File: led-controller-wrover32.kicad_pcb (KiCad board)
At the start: 4 copper layers, 36 x 40 mm, 123 parts, among them J101 Micro USB, J102 UART, J103 STATUS OUT, J104 USB_B_Micro, J105 POWER IN, J107 I2C, J108 5V_LOGIC, J303 Micro_SD_Card, J304 Speaker, J401 Fan PWM, J402 GPIO_CONN, J409 12V_OUT, Q101 UMH3N, Q102 BSS138, Q103 EM6K7T2R, Q303 BSS138, Q401 SIL2301-TP, Q402 EM6K7T2R, SW301 KMR2, SW302 KMR2, U102 USBUF02W6, U103 ESP32-S3-WROOM-2-N32R8V, U104 MAX3379EETD, U105 AP22815AWT-7, U201 XCL220, U301 SSM2518CPZ, U401 BNO085, U402 PCA9575HF, U405 TPS55340-Q1, Y401 OM-7604-C7

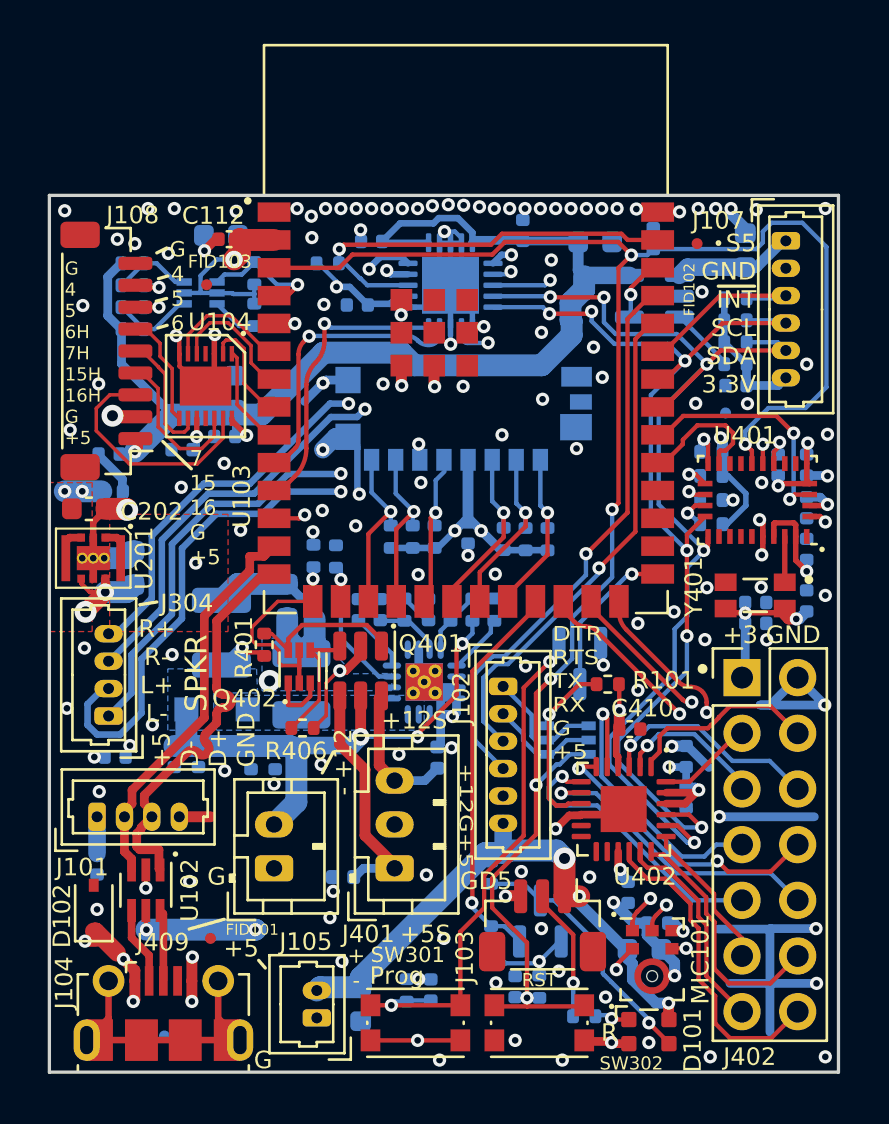
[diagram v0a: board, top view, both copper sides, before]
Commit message: More updates
- Changed obsolete unidirectional level shifter to open-collector level shifter
- Replaced BSS138 level shifters with dedicated level shifter
- Changed all 5V I/O pins to have 33 ohm resistor in series
- Changed a few capacitors
- Cleanup tracks, vias, silkscreen, etc.

Signed-off-by: Aaron Williams <aaron.w2@gmail.com>
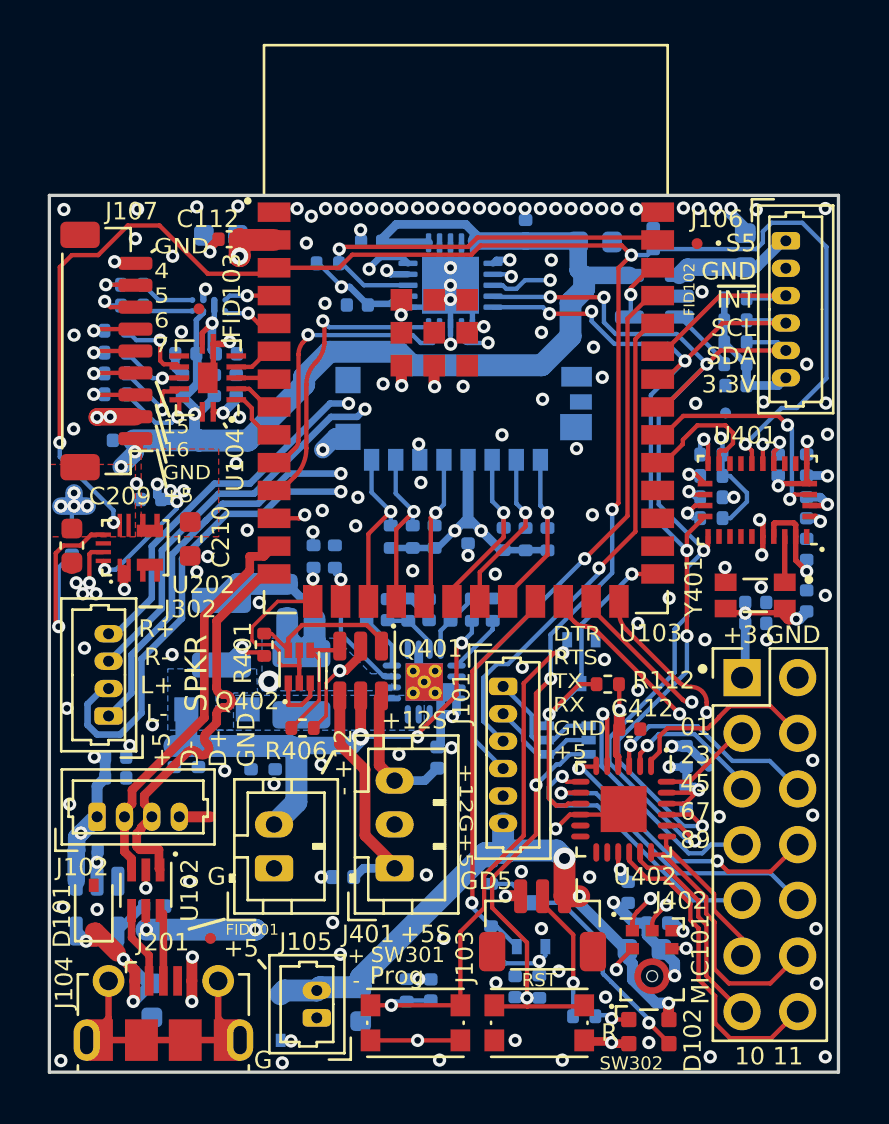
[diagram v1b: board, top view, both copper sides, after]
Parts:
- removed the C108 at (68.5, 39.0)
- removed the C201 at (63.9, 47.0)
- removed the C202 at (61.8, 44.3)
- removed Q103: EM6K7T2R, Package_TO_SOT_SMD:SOT-563
- removed the R109 at (69.3, 33.5)
- removed the R110 at (63.8, 33.1)
- removed the R112 at (69.3, 35.5)
- removed the R113 at (63.8, 36.1)
- removed the U201 at (62.0, 46.5)
- added C103: 0.1uF, Capacitor_SMD:C_0402_1005Metric, B.Cu at (61.7, 59.9)
- added C104: 10uF, Capacitor_SMD:C_0603_1608Metric, B.Cu at (64.7, 66.7)
- added C105: 0.1uF, Capacitor_SMD:C_0402_1005Metric, B.Cu at (64.8, 62.4)
- added C110: 1uF, Capacitor_SMD:C_0402_1005Metric, B.Cu at (66.1, 38.7)
- added C115: 1uF, Capacitor_SMD:C_0402_1005Metric, B.Cu at (68.1, 37.2)
- added C116: 1uF, Capacitor_SMD:C_0402_1005Metric, B.Cu at (66.2, 37.2)
- added C209: 22uF, Capacitor_SMD:C_0603_1608Metric, F.Cu at (61.0, 46.0)
- added C210: 22uF, Capacitor_SMD:C_0603_1608Metric, F.Cu at (66.4, 45.7)
- added D103: UDD32C12L01, Diode_SMD:D_SOD-323, B.Cu at (70.5, 67.5)
- added R104: 33, Resistor_SMD:R_0402_1005Metric, B.Cu at (63.0, 39.1)
- added R105: 33, Resistor_SMD:R_0402_1005Metric, B.Cu at (63.0, 38.1)
- added R106: 33, Resistor_SMD:R_0402_1005Metric, B.Cu at (63.0, 37.2)
- added R107: 33, Resistor_SMD:R_0402_1005Metric, B.Cu at (63.0, 36.2)
- added R206: 10K, Resistor_SMD:R_0402_1005Metric, B.Cu at (61.0, 45.9)
- added U101: AP2191WG-7, Package_TO_SOT_SMD:SOT-23-5, B.Cu at (62.2, 62.4)
- added U106: TCA9406ZYPR, Package_BGA:Texas_DSBGA-8_0.9x1.9mm_Layout2x4_P0.5mm, B.Cu at (67.3, 35.0)
- added U202: MPM3810GQB-33, Package_DFN_QFN:Monolithic_QFN-12-2.5x3.0mm_P0.4mm, F.Cu at (63.9, 46.1)
- J102: renamed from J101; value Micro USB -> USB
- Q102: footprint Package_TO_SOT_SMD:SOT-23 -> Package_TO_SOT_SMD:SOT-323_SC-70
- Q301: renamed from Q303; footprint Package_TO_SOT_SMD:SOT-23 -> Package_TO_SOT_SMD:SOT-323_SC-70
- R113: renamed from R111; value 22 -> 33
- R114: value 22 -> 33
- U104: value MAX3379EETD -> NTS0104BQ,115; footprint Aaron:TDFN-14_3x3mm_P0.4mm_EP1.78x2.35mm -> Package_TO_SOT_SMD:SOT-762-1
- U402: footprint Package_DFN_QFN:HVQFN-24-1EP_4x4mm_P0.5mm_EP2.1x2.1mm -> Aaron:HWQFN-24_EP_4x4_Pitch0.5mm
- moved C106 4.02 mm to (63.0, 56.6), turned to 0 degrees
- moved C108 3.83 mm to (68.5, 38.7), turned to 90 degrees
- moved C109 2.37 mm to (67.5, 38.7), turned to 90 degrees
- moved C211 1.79 mm to (64.6, 43.9), turned to 180 degrees
- moved FID103 1.15 mm to (66.8, 35.2)
- moved FID105 1.08 mm to (66.3, 68.3)
- moved R114 1.03 mm to (63.8, 34.1), turned to 0 degrees
- moved R113 0.93 mm to (63.8, 35.0), turned to 0 degrees
- moved C118 0.90 mm to (63.4, 41.2)
- moved Q102 0.46 mm to (82.0, 63.3)
- moved U104 0.39 mm to (67.2, 38.3), turned to 90 degrees
- moved C206 0.38 mm to (74.5, 48.9)
- moved C207 0.33 mm to (75.4, 48.9)
- moved R405 0.27 mm to (90.2, 44.7)
- moved R205 0.17 mm to (76.4, 48.9)
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- renumbered C116 to C101, C104 to C102, C105 to C106, C106 to C107, C110 to C108, C115 to C117, C117 to C118, C416 to C201, C417 to C202, C418 to C203, C419 to C204, C420 to C205, C421 to C206, C422 to C207, C423 to C208, C203 to C211, C314 to C301, C315 to C302, C316 to C303, C303 to C304, C318 to C305, C301 to C306, C302 to C307, C319 to C308, C412 to C410, C413 to C411, C410 to C412, C411 to C413, D102 to D101, D101 to D102, D402 to D201, D403 to D402, J102 to J101, J107 to J106, J108 to J107, J409 to J201, J303 to J301, J304 to J302, L401 to L201, R102 to R101, R103 to R102, R104 to R103, R105 to R109, R106 to R110, R107 to R111, R101 to R112, R416 to R201, R115 to R202, R417 to R203, R418 to R204, R419 to R205, R308 to R301, R309 to R305, R305 to R306, R306 to R307, R307 to R308, R301 to R309, U405 to U201
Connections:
- net /DO renamed /STS_DO
- net /IO2 renamed /SW_5V_EN
- net /IO46_5V renamed /STS_5V
- C101 pad 1: PVDD -> +5V
- C102 pad 1: PVDD -> +5V
- C106 pad 1: PVDD -> +5V
- C107 pad 1: PVDD -> +5V
- C109 pad 1: PVDD -> +5V
- C118 pad 1: PVDD -> +5V
- C204 pad 1: PVDD -> +5V
- C205 pad 1: PVDD -> +5V
- C305 pad 1: PVDD -> +5V
- C306 pad 1: PVDD -> +5V
- C307 pad 1: PVDD -> +5V
- D101 pad 1: PVDD -> VBUS
- D102 pad 4: PVDD -> +5V
- J101 pad 6: PVDD -> +5V
- J102 pad 1: PVDD -> +5V
- J103 pad 1: PVDD -> +5V
- J104 pad 1: PVDD -> VBUS
- J105 pad 2: PVDD -> +5V
- J107 pad 1: PVDD -> +5V
- L201 pad 1: PVDD -> +5V
- Q401 pad 2: PVDD -> +5V
- R102 pad 2: PVDD -> +5V
- R113 pad 1: /IO4_H -> /IO5_H
- R114 pad 1: /IO5_H -> /IO4_H
- R406 pad 1: PVDD -> +5V
- U104 pad 1: IO16 -> +3V3
- U104 pad 10: +3V3 -> Net-(R107-Pad2)
- U104 pad 11: unconnected-(U104-Pad11) -> Net-(R106-Pad2)
- U104 pad 12: /IO15_H -> Net-(R105-Pad2)
- U104 pad 13: /IO16_H -> Net-(R104-Pad2)
- U104 pad 14: PVDD -> +5V
- U104 pad 2: /IO15 -> IO16
- U104 pad 3: GND -> /IO15
- U104 pad 4: unconnected-(U104-Pad4) -> /IO7
- U104 pad 5: /IO7 -> /IO6
- U104 pad 6: /IO6 -> unconnected-(U104-Pad6)
- U104 pad 8: /IO6_H -> +3V3
- U104 pad 9: /IO7_H -> unconnected-(U104-Pad9)
- U105 pad 5: PVDD -> +5V
- U201 pad 2: PVDD -> +5V
- U301 pad 16: PVDD -> +5V
- U301 pad 20: PVDD -> +5V
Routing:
- net PVDD: track 99.4 -> 0.00 mm, vias 13 -> 0
- net +5V: track 0.00 -> 96.9 mm, vias 0 -> 14
- net GND: track 106.1 -> 70.1 mm, vias 143 -> 159
- net ~{RESET}: track 85.4 -> 108.6 mm, vias 6 -> 8
- net VBUS: track 0.00 -> 11.1 mm, vias 0 -> 3
- net /Power Supplies/EN_5V: track 0.00 -> 9.46 mm, vias 0 -> 1
- net /IO16_H: track 10.9 -> 2.40 mm, vias 0 -> 1
- net /IO15_H: track 6.77 -> 2.40 mm, vias 0 -> 1
- net /IO7: track 5.81 -> 1.67 mm
- net Net-(R105-Pad2): track 0.00 -> 3.95 mm, vias 0 -> 1
- net Net-(R104-Pad2): track 0.00 -> 3.78 mm, vias 0 -> 1
- net /IO6: track 5.49 -> 1.72 mm
- net Net-(R107-Pad2): track 0.00 -> 3.62 mm, vias 0 -> 1
- net /IO15: track 5.21 -> 1.76 mm
- net /IO7_H: track 5.48 -> 2.42 mm, vias 0 -> 1
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- added copper zone on B.Cu, net +5V
- added copper zone on F.Cu, net +5V
- added copper zone on In2.Cu, net +5V
- removed copper zone on F.Cu, net (none)
- removed copper zone on B.Cu, net PVDD
- removed copper zone on In2.Cu, net PVDD
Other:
- board text added: "01 23 45 67 89"
- board text added: "10 11"
- board text added: "15 16 GND +5"
- board text added: "DTR RTS TX RX GND +5"
- board text added: "GND 4 5 6 7"
- board text removed: "+5 GND"
- board text removed: "7 15 16 G +5"
- board text removed: "DTR RTS TX RX G +5"
- board text removed: "G 4 5 6"
- board text removed: "G 4 5 6H 7H 15H 16H G +5"

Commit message: Multiple updates
- Changed input current limiter to ferrite bead
- Added pull-up for BNO085 boot mode
- Minor layout changes

Signed-off-by: Aaron Williams <aaron.w2@gmail.com>
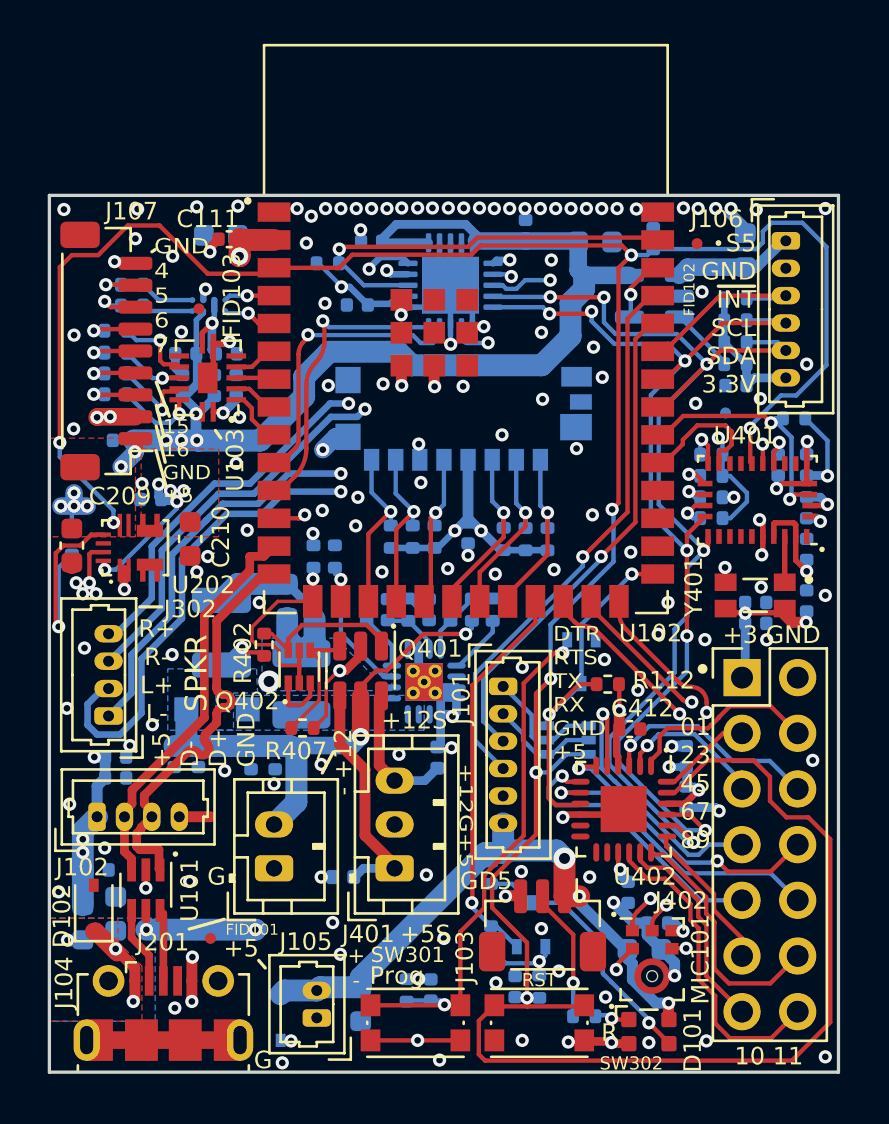
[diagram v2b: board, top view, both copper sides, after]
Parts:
- removed the C103 at (61.7, 59.9)
- removed the U101 at (62.2, 62.4)
- added FB101: 2A 300 ohm@100MHz, Inductor_SMD:L_0603_1608Metric, B.Cu at (61.5, 63.2)
- added R401: 10K, Resistor_SMD:R_0402_1005Metric, B.Cu at (94.0, 40.2)
- moved C103 4.28 mm to (63.0, 62.8), turned to 90 degrees
- moved C104 3.06 mm to (62.2, 60.8)
- renumbered C104 to C103, C105 to C104, C106 to C105, C107 to C106, C108 to C107, C109 to C108, C110 to C109, C111 to C110, C112 to C111, C113 to C112, C114 to C113, C115 to C114, C116 to C115, C117 to C116, C118 to C117, D102 to D101, D101 to D102, R401 to R402, R402 to R403, R403 to R404, R404 to R405, R405 to R406, R406 to R407, R407 to R408, U102 to U101, U103 to U102, U104 to U103, U105 to U104, U106 to U105
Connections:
- C104 pad 1: VBUS -> +5V
- U402 pad 23: +3V3 -> ~{RESET}
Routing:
- net ~{RESET}: track 108.6 -> 146.2 mm
- net VBUS: track 11.1 -> 5.32 mm
- net +12V: track 27.5 -> 25.1 mm, vias 4 -> 3
- net +3V3: track 88.1 -> 90.0 mm
- net +5V: track 96.9 -> 98.0 mm, vias 14 -> 18
- net GND: track 70.1 -> 70.0 mm, vias 159 -> 154
- added copper zone on B.Cu, net VBUS
- added copper zone on F.Cu, net VBUS
- added copper zone on In2.Cu, net VBUS

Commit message: More updates
- Removed 5V switch
- Added manual reset control of BNO085 to support booting remotely
- More minor cleanups
- Added jpeg renderings

Signed-off-by: Aaron Williams <aaron.w2@gmail.com>
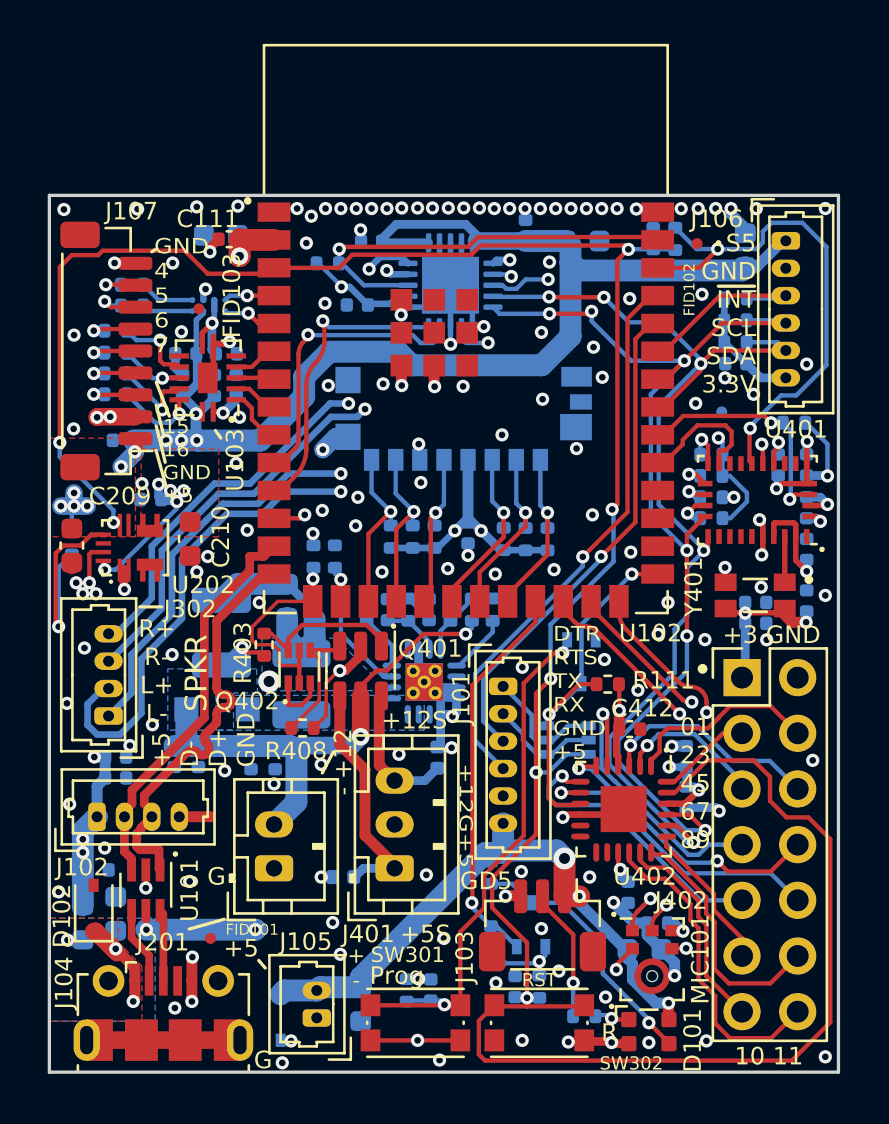
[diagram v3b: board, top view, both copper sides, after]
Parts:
- removed the R108 at (91.3, 37.7)
- removed the U104 at (87.6, 34.6)
- added R401: 10K, Resistor_SMD:R_0402_1005Metric, B.Cu at (88.6, 32.0)
- J101: value UART -> Molex PicoBlade 6-pin
- J102: value USB -> Molex PicoBlade 4-pin
- J106: value I2C -> Molex PicoBlade 6-pin
- J302: value Speaker -> Molex PicoBlade 4-pin
- R103: value 22 -> 33
- moved C113 1.00 mm to (91.3, 37.7)
- moved C306 0.58 mm to (84.3, 32.1)
- moved R402 0.20 mm to (94.0, 40.4)
- moved FID106 0.18 mm to (90.7, 39.9)
- renumbered R109 to R108, R110 to R109, R111 to R110, R112 to R111, R113 to R112, R114 to R113, R401 to R402, R402 to R403, R403 to R404, R404 to R405, R405 to R406, R406 to R407, R407 to R408, R408 to R409, U105 to U104
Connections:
- C112 pad 1: Net-(C112-Pad1) -> +5V
- J106 pad 1: Net-(C112-Pad1) -> +5V
- U102 pad 38: /SW_5V_EN -> ~{RST_BNO085}
- U401 pad 11: ~{RESET} -> ~{RST_BNO085}
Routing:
- net ~{RST_BNO085}: track 0.00 -> 23.4 mm, vias 0 -> 2
- net ~{RESET}: track 146.2 -> 125.4 mm, vias 8 -> 7
- net +5V: track 98.0 -> 105.6 mm
- net Net-(C112-Pad1): track 5.37 -> 0.00 mm
- net Net-(R108-Pad2): track 2.87 -> 0.00 mm
- net /SW_5V_EN: track 2.57 -> 0.00 mm, vias 1 -> 0
- net +3V3: track 90.0 -> 88.8 mm
- net ~{M_BOOT_LOAD}: track 11.0 -> 10.1 mm
- net SDA: track 49.7 -> 48.9 mm
- net GND: track 70.0 -> 70.3 mm, vias 154 -> 155
